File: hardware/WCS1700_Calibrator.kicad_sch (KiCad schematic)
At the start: 77 parts, among them J1 PJ-002B, J2 560020-0330, J3 282834-8, J4 Conn_01x03_Pin, J5 282834-6, Q1 AO3422, Q2 AO3422, Q3 AO3422, Q4 AO3422, Q5 AO3422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

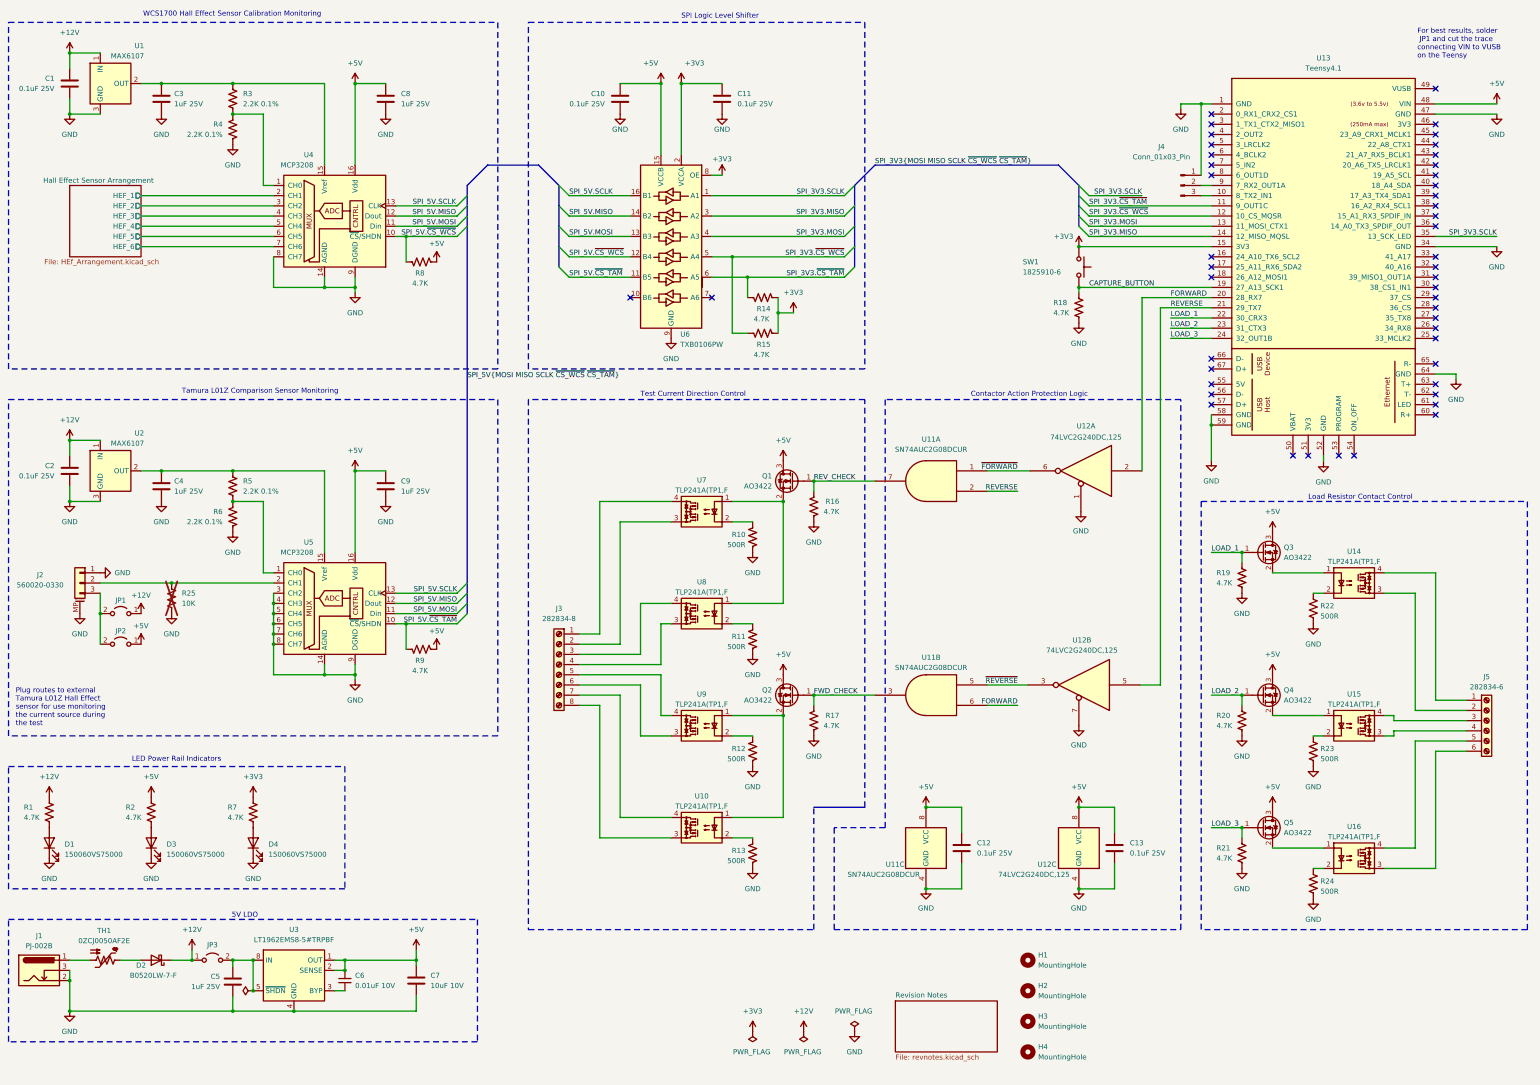
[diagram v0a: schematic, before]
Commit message: Edited schematic to relocated FETs as proper low-side switches
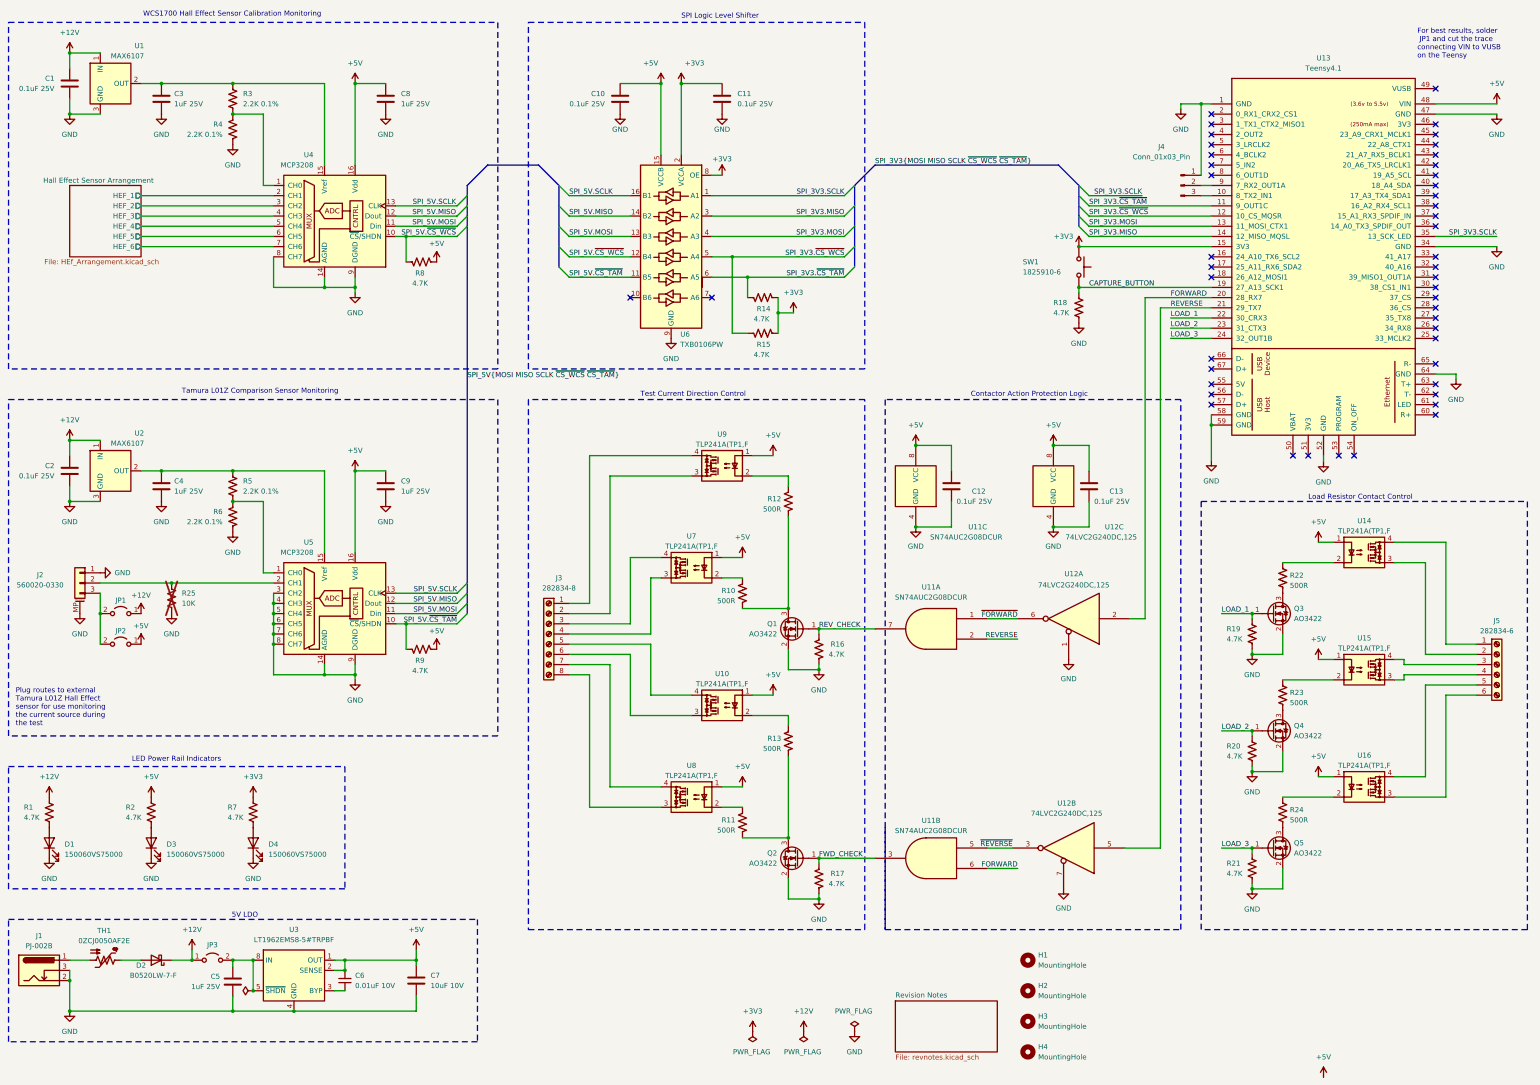
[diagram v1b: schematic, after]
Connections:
- net +5V: now also U10.1, U14.1, U15.1, U16.1, U7.1, U8.1, U9.1; no longer Q1.3 (D), Q2.3 (D), Q3.3 (D), Q4.3 (D), Q5.3 (D)
- net GND: now also Q1.2 (S), Q2.2 (S), Q3.2 (S), Q4.2 (S), Q5.2 (S); no longer R10.2, R11.2, R12.2, R13.2, R22.2, R23.2, R24.2
- net at U10.3: now also J3.6 (Pin_6); no longer J3.8 (Pin_8)
- net at U10.4: now also J3.5 (Pin_5); no longer J3.7 (Pin_7)
- net at J3.2 (Pin_2): now also U9.3; no longer U7.3
- net at J3.1 (Pin_1): now also U9.4; no longer U7.4
- net at U8.4: now also J3.7 (Pin_7); no longer J3.3 (Pin_3)
- net at U8.3: now also J3.8 (Pin_8); no longer J3.4 (Pin_4)
- new net: Q2.3 (D), R11.2, R13.2
- new net: Q5.3 (D), R24.2
- new net: Q4.3 (D), R23.2
- new net: Q1.3 (D), R10.2, R12.2
- new net: J3.3 (Pin_3), U7.4
- new net: J3.4 (Pin_4), U7.3
- new net: Q3.3 (D), R22.2
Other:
- moved on the sheet: J5, Q1, Q2, Q3, Q4, Q5, R16, R17, R19, R20, R21, R22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
